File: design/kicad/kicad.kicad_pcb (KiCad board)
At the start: 2 copper layers, 65 x 56 mm, 19 parts, among them J1 Raspberry_Pi_4, J2 Conn_01x05, J3 Conn_01x05, J4 Conn_01x08, Q1 AO3401A, Q2 AO3401A, Q3 AO3401A, SW1 SW_Shutdown

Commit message: prod update
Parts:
- added D4: BUZY, easyeda2kicad:LED-TH_BD3.9-P2.54-FD, F.Cu at (177.0, 95.2)
- added D5: BATTERY, easyeda2kicad:LED-TH_BD3.9-P2.54-FD, F.Cu at (149.0, 95.0)
- added D6: SD_CARD, easyeda2kicad:LED-TH_BD3.9-P2.54-FD, F.Cu at (161.7, 95.0)
- D1: value LED_BUZY (Yellow) -> BUZY; footprint LED_THT:LED_D3.0mm_Horizontal_O1.27mm_Z2.0mm -> easyeda2kicad:LED-SMD_L1.7-W0.6-RD-custom; moved to F.Cu
- D2: value LED_BATTERY (Red) -> BATTERY; footprint LED_THT:LED_D3.0mm_Horizontal_O1.27mm_Z2.0mm -> easyeda2kicad:LED-SMD_L1.7-W0.6-RD-custom; moved to F.Cu
- D3: value LED_SD_CARD (Blue) -> SD_CARD; footprint LED_THT:LED_D3.0mm_Horizontal_O1.27mm_Z2.0mm -> easyeda2kicad:LED-SMD_L1.7-W0.6-RD-custom; moved to F.Cu
- J1: footprint Connector_PinSocket_2.54mm:PinSocket_2x20_P2.54mm_Vertical -> easyeda2kicad:HDR-TH_40P-P2.54-V-F-R2-C20-S2.54-2-reveresed
- J2, J3: footprint Connector_JST:JST_PH_S5B-PH-K_1x05_P2.00mm_Horizontal -> easyeda2kicad:CONN-TH_WAFER-HA254WZ-5A
- Q1, Q2, Q3: value AO3401A -> AO3400A; footprint Package_TO_SOT_SMD:SOT-23W -> easyeda2kicad:SOT-23-3_L2.9-W1.3-P1.90-LS2.4-BR
- R4, R7, R8: value 500 -> 220
- SW1: footprint Button_Switch_THT:SW_Tactile_SPST_Angled_PTS645Vx83-2LFS -> easyeda2kicad:SW-TH_TK-6580B-2; moved to F.Cu
- moved J1 24.2 mm to (157.1, 47.5), turned to 0 degrees
- moved R4 9.35 mm to (174.0, 85.5)
- moved R8 8.90 mm to (143.5, 85.6)
- moved Q1 8.35 mm to (183.0, 85.5)
- moved R7 8.15 mm to (157.5, 85.5)
- moved Q2 8.10 mm to (152.5, 85.5)
- moved Q3 8.05 mm to (166.0, 85.5)
- moved SW1 7.26 mm to (140.8, 93.4)
- moved J2 7.13 mm to (132.4, 77.0)
- moved J3 4.97 mm to (132.4, 61.0)
- moved D2 3.20 mm to (149.0, 99.2)
- moved D3 2.85 mm to (161.7, 99.2)
- moved D1 2.67 mm to (177.0, 99.2)
- moved R2 1.30 mm to (178.1, 85.5)
- moved R1 1.08 mm to (136.3, 85.7)
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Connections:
- Q1 pad 2: +5V -> GND
- Q1 pad 3: Net-(D1-A) -> Net-(D1-K)
- Q2 pad 2: +5V -> GND
- Q2 pad 3: Net-(D2-A) -> Net-(D2-K)
- Q3 pad 2: +5V -> GND
- Q3 pad 3: Net-(D3-A) -> Net-(D3-K)
- R4 pad 1: Net-(D1-K) -> Net-(D1-A)
- R4 pad 2: GND -> +5V
- R7 pad 1: Net-(D3-K) -> Net-(D3-A)
- R7 pad 2: GND -> +5V
- R8 pad 1: Net-(D2-K) -> Net-(D2-A)
- R8 pad 2: GND -> +5V
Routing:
- net +5V: track 0.00 -> 115.4 mm, vias 0 -> 4
- net RST_BTN: track 0.00 -> 69.8 mm, vias 0 -> 1
- net GPS_STATUS: track 0.00 -> 67.4 mm
- net +3.3V: track 0.00 -> 56.2 mm, vias 0 -> 1
- net LED_BUZY: track 0.00 -> 45.4 mm
- net LED_BATTERY: track 0.00 -> 43.8 mm
- net SENSOR1_RX: track 0.00 -> 40.7 mm
- net SENSOR2_TX: track 0.00 -> 39.7 mm, vias 0 -> 1
- net SENSOR2_RX: track 0.00 -> 38.7 mm, vias 0 -> 1
- net LED_SD_CARD: track 0.00 -> 38.0 mm
- net SENSOR1__TX: track 0.00 -> 32.8 mm
- net SENSOR3_RX: track 0.00 -> 30.8 mm
- net SENSOR3__TX: track 0.00 -> 26.0 mm
- net Net-(D1-K): track 0.00 -> 16.3 mm
- net Net-(D3-K): track 0.00 -> 15.5 mm
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- added copper zone on B.Cu, net GND
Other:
- board text added: "+"
- board text added: "-"
- board text added: "CYCLSOSAFE"
- board text removed: "CYCLOSAFE PROJECT"

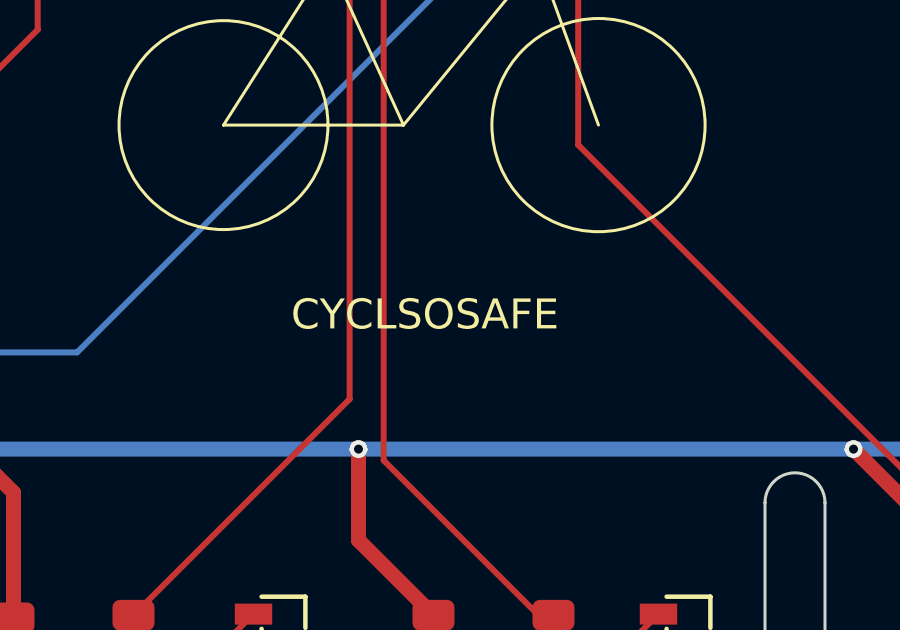
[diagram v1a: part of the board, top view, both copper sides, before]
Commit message: edited library path for kicad symbol
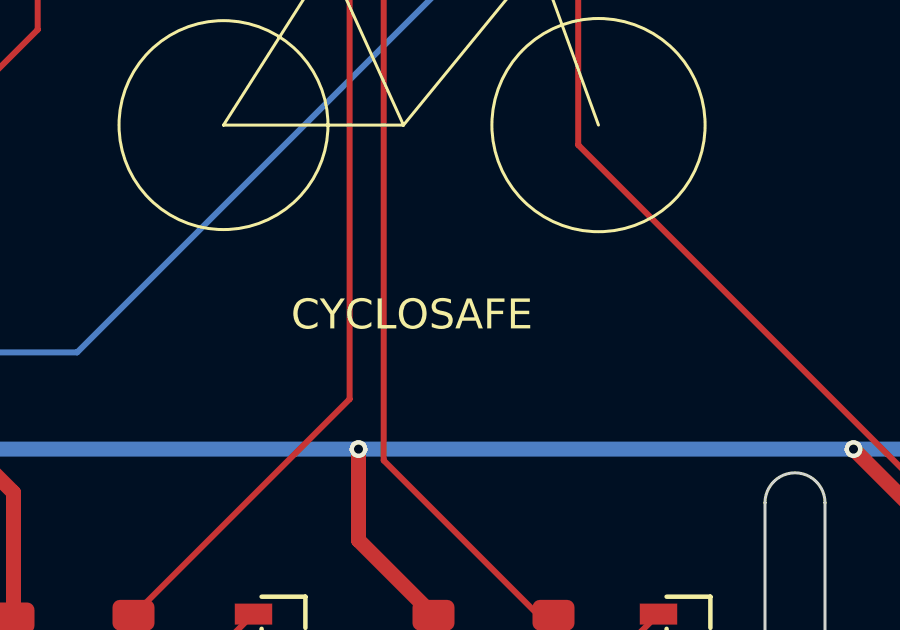
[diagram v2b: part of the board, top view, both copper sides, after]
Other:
- board text added: "CYCLOSAFE"
- board text removed: "CYCLSOSAFE"
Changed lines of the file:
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@@
 			(psa4output no)
 			(plot_black_and_white yes)
+			(plotinvisibletext no)
 			(sketchpadsonfab no)
 			(plotpadnumbers no)
@@
 		)
 		(embedded_fonts no)
-		(model "C:/Users/npirard.IGN/Documents/cyclosafe/design/kicad/libs/easyeda2kicad/easyeda2kicad.3dshapes/SOT-23-3P_L2.9-W1.3-H1.0-LS2.4-P0.95.wrl"
+		(model "${KIPRJMOD}/libs/easyeda2kicad/easyeda2kicad.3dshapes/SOT-23-3P_L2.9-W1.3-H1.0-LS2.4-P0.95.wrl"
 			(offset
-				(xyz -861.57 843.28 -0)
+				(xyz 0 0 -0)
 			)
 			(scale
@@
 			)
 			(rotate
-				(xyz 0 0 180)
+				(xyz -0 -0 180)
 			)
 		)
@@
 		)
 		(embedded_fonts no)
-		(model "C:/Users/npirard.IGN/Documents/cyclosafe/design/kicad/libs/easyeda2kicad/easyeda2kicad.3dshapes/LED-SMD_L1.7-W0.6-H1.2.wrl"
+		(model "${KIPRJMOD}/libs/easyeda2kicad/easyeda2kicad.3dshapes/LED-SMD_L1.7-W0.6-H1.2.wrl"
 			(offset
 				(xyz -0 -0.36 0.3)
@@
 		)
 		(embedded_fonts no)
-		(model "C:/Users/npirard.IGN/Documents/cyclosafe/design/kicad/libs/easyeda2kicad/easyeda2kicad.3dshapes/SOT-23-3P_L2.9-W1.3-H1.0-LS2.4-P0.95.wrl"
+		(model "${KIPRJMOD}/libs/easyeda2kicad/easyeda2kicad.3dshapes/SOT-23-3P_L2.9-W1.3-H1.0-LS2.4-P0.95.wrl"
 			(offset
-				(xyz -861.57 843.28 -0)
+				(xyz 0 0 -0)
 			)
 			(scale
@@
 			)
 			(rotate
-				(xyz 0 0 180)
+				(xyz -0 -0 180)
 			)
 		)
@@
 		)
 		(embedded_fonts no)
-		(model "C:/Users/npirard.IGN/Documents/cyclosafe/design/kicad/libs/easyeda2kicad/easyeda2kicad.3dshapes/SW-TH_TK-6580B-2.wrl"
+		(model "${KIPRJMOD}/libs/easyeda2kicad/easyeda2kicad.3dshapes/SW-TH_TK-6580B-2.wrl"
 			(offset
 				(xyz 0 -5.85 0)
@@
 		)
 		(embedded_fonts no)
-		(model "C:/Users/npirard.IGN/Documents/cyclosafe/design/kicad/libs/easyeda2kicad/easyeda2kicad.3dshapes/SOT-23-3P_L2.9-W1.3-H1.0-LS2.4-P0.95.wrl"
+		(model "${KIPRJMOD}/libs/easyeda2kicad/easyeda2kicad.3dshapes/SOT-23-3P_L2.9-W1.3-H1.0-LS2.4-P0.95.wrl"
 			(offset
-				(xyz -861.57 843.28 -0)
+				(xyz 0 0 -0)
 			)
 			(scale
@@
 			)
 			(rotate
-				(xyz 0 0 180)
+				(xyz -0 -0 180)
 			)
 		)
@@
 		)
 		(embedded_fonts no)
-		(model "C:/Users/npirard.IGN/Documents/cyclosafe/design/kicad/libs/easyeda2kicad/easyeda2kicad.3dshapes/LED-SMD_L1.7-W0.6-H1.2.wrl"
+		(model "${KIPRJMOD}/libs/easyeda2kicad/easyeda2kicad.3dshapes/LED-SMD_L1.7-W0.6-H1.2.wrl"
 			(offset
 				(xyz -0 -0.36 0.3)
@@
 		)
 		(embedded_fonts no)
-		(model "C:/Users/npirard.IGN/Documents/cyclosafe/design/kicad/libs/easyeda2kicad/easyeda2kicad.3dshapes/CONN-TH_WAFER-HA254WZ-5A.wrl"
+		(model "${KIPRJMOD}/libs/easyeda2kicad/easyeda2kicad.3dshapes/CONN-TH_WAFER-HA254WZ-5A.wrl"
 			(offset
 				(xyz 0 -0.4 2.9)
@@
 		)
 		(embedded_fonts no)
-		(model "C:/Users/npirard.IGN/Documents/cyclosafe/design/kicad/libs/easyeda2kicad/easyeda2kicad.3dshapes/CONN-TH_WAFER-HA254WZ-5A.wrl"
+		(model "${KIPRJMOD}/libs/easyeda2kicad/easyeda2kicad.3dshapes/CONN-TH_WAFER-HA254WZ-5A.wrl"
 			(offset
 				(xyz 0 -0.4 2.9)
@@
 		)
 		(embedded_fonts no)
-		(model "C:/Users/npirard.IGN/Documents/cyclosafe/design/kicad/libs/easyeda2kicad/easyeda2kicad.3dshapes/LED-SMD_L1.7-W0.6-H1.2.wrl"
+		(model "${KIPRJMOD}/libs/easyeda2kicad/easyeda2kicad.3dshapes/LED-SMD_L1.7-W0.6-H1.2.wrl"
 			(offset
 				(xyz -0 -0.36 0.3)
@@
 		)
 		(embedded_fonts no)
-		(model "C:/Users/npirard.IGN/Documents/cyclosafe/design/kicad/libs/easyeda2kicad/easyeda2kicad.3dshapes/HDR-TH_40P-P2.54-V-F-R2-C20-S2.54-2.wrl"
+		(model "${KIPRJMOD}/libs/easyeda2kicad/easyeda2kicad.3dshapes/HDR-TH_40P-P2.54-V-F-R2-C20-S2.54-2.wrl"
 			(offset
 				(xyz 0 -0 2.1)
@@
 		)
 	)
-	(gr_text "CYCLSOSAFE"
+	(gr_text "CYCLOSAFE"
 		(at 152.75 75.15 0)
 		(layer "F.SilkS")
